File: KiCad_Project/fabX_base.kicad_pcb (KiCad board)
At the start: 2 copper layers, 62 x 62 mm, 42 parts, among them J1 SolderJumper_2_Open, J2 SolderJumper_2_Open, J3 SolderJumper_2_Open, J4 SolderJumper_2_Open, J5 SolderJumper_2_Open, J6 SolderJumper_2_Open, Q5 BCX19, Q6 BCX19, U1 MCP23008, U2 MCP23008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

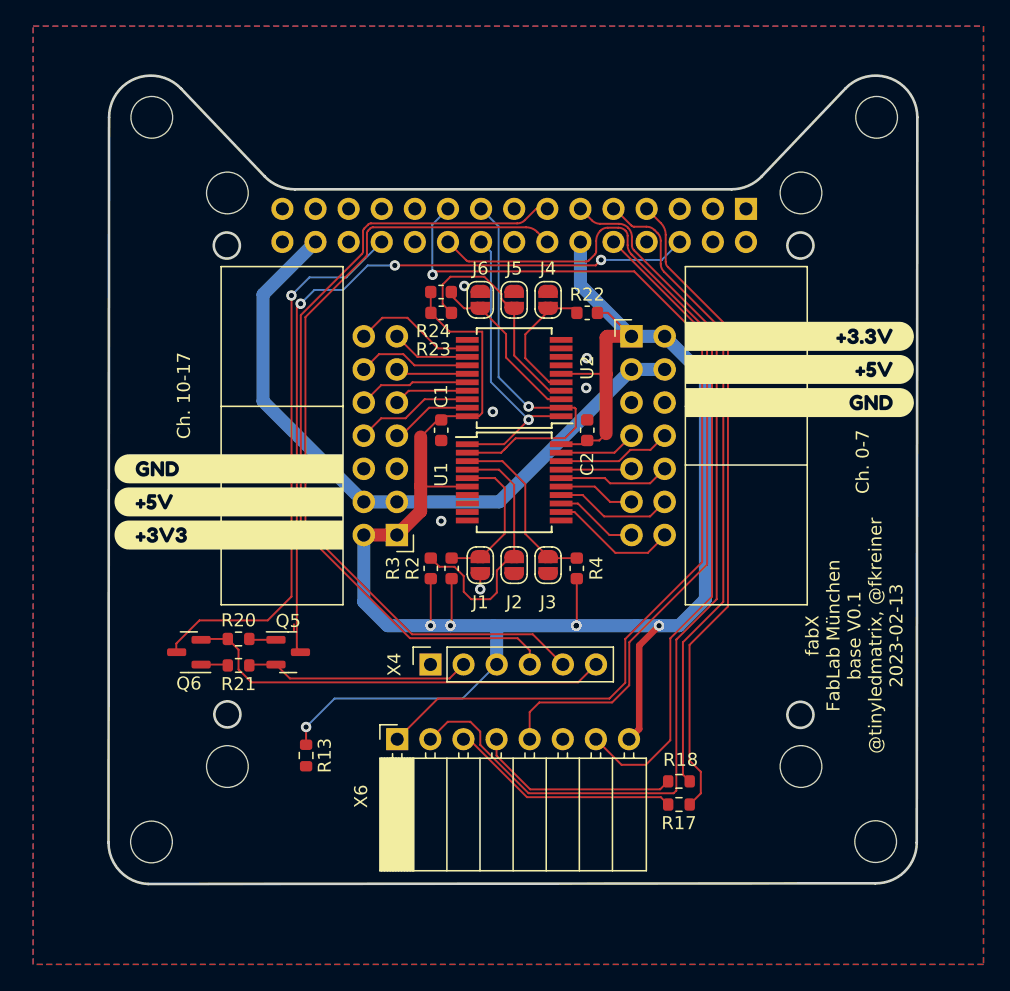
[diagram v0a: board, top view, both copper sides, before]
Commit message: add pulldowns to inputs
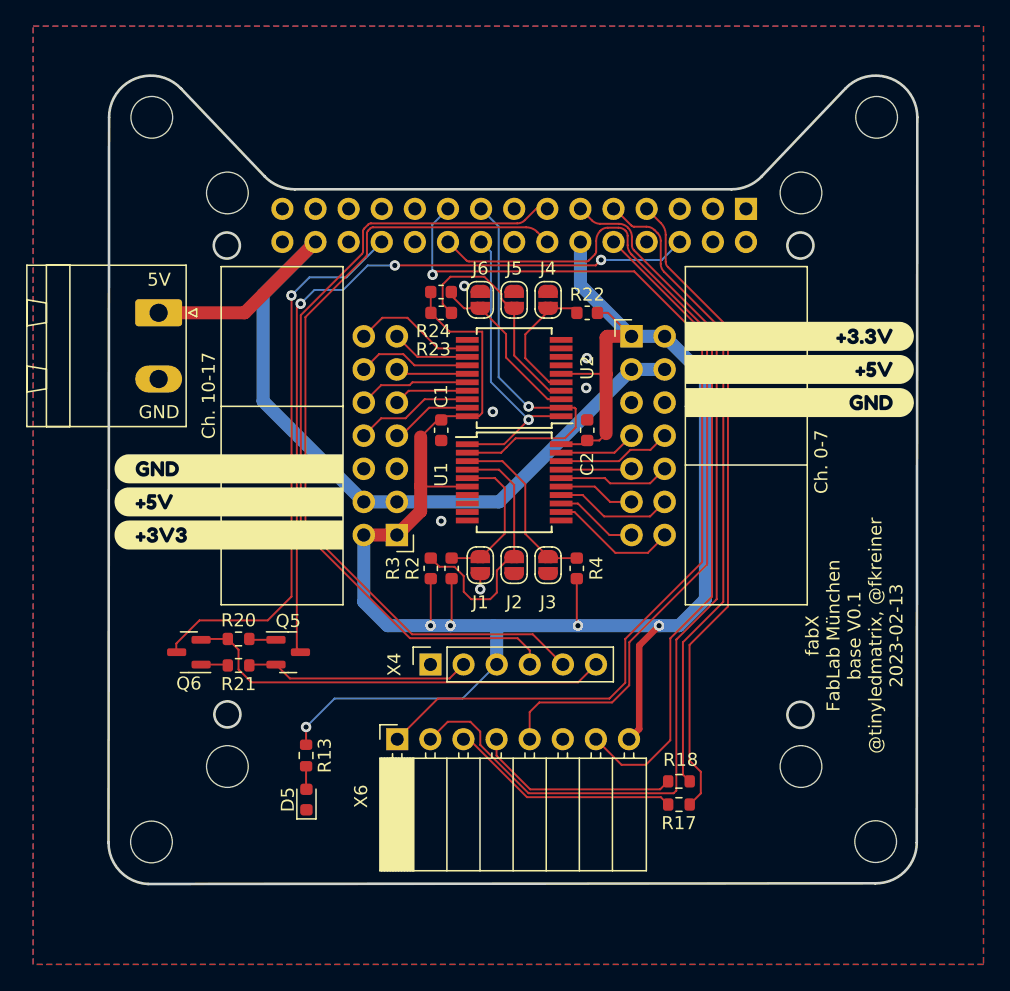
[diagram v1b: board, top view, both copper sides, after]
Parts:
- added D5: LED, LED_SMD:LED_0603_1608Metric, F.Cu at (134.0, 117.1)
- added X2: Screw_Terminal_01x02, Connector_Phoenix_MSTB:PhoenixContact_MSTBA_2,5_2-G-5,08_1x02_P5.08mm_Horizontal, F.Cu at (122.6, 79.8)
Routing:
- net +5V: track 52.1 -> 66.4 mm
- net Net-(D5-Pad2): track 0.00 -> 1.78 mm
- net /coreRST: track 58.7 -> 58.2 mm
- net +3V3: track 160.0 -> 159.7 mm, vias 6 -> 5
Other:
- board text added: "5V"
- board text added: "GND"

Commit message: place pulldowns
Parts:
- added R1: 100k, Resistor_SMD:R_0603_1608Metric, F.Cu at (128.7, 103.7)
- added R10: 100k, Resistor_SMD:R_0603_1608Metric, F.Cu at (137.8, 103.7)
- added R11: 100k, Resistor_SMD:R_0603_1608Metric, F.Cu at (139.3, 103.7)
- added R5: 100k, Resistor_SMD:R_0603_1608Metric, F.Cu at (130.2, 103.7)
- added R6: 100k, Resistor_SMD:R_0603_1608Metric, F.Cu at (131.7, 103.7)
- added R7: 100k, Resistor_SMD:R_0603_1608Metric, F.Cu at (133.2, 103.7)
- added R8: 100k, Resistor_SMD:R_0603_1608Metric, F.Cu at (134.7, 103.7)
- added R9: 100k, Resistor_SMD:R_0603_1608Metric, F.Cu at (136.3, 103.7)
- moved Q5 10.5 mm to (122.0, 105.1), turned to 90 degrees
- moved R20 8.75 mm to (121.0, 108.9), turned to 90 degrees
- moved Q6 7.49 mm to (122.0, 112.7), turned to -90 degrees
- moved R21 6.06 mm to (123.1, 108.9), turned to -90 degrees
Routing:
- net /Ch11: track 6.05 -> 34.5 mm
- net /Ch10: track 9.50 -> 37.1 mm
- net /Ch13: track 5.54 -> 29.0 mm
- net /Ch12: track 8.78 -> 31.4 mm
- net /Ch15: track 5.77 -> 24.8 mm
- net /Ch14: track 8.58 -> 26.3 mm
- net RX: track 62.2 -> 79.4 mm
- net TX: track 63.1 -> 80.2 mm
- net /Ch17: track 6.29 -> 23.2 mm
- net GND: track 1.20 -> 17.0 mm, vias 6 -> 17
- net /Ch16: track 9.10 -> 23.7 mm
- net /G0(BOOT): track 42.7 -> 51.7 mm
- net CTS: track 17.4 -> 25.6 mm
- net DTR: track 33.2 -> 38.5 mm
- net /coreRST: track 58.2 -> 62.3 mm
